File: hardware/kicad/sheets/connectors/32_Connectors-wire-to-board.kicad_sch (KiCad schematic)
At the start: 46 parts

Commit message: reorganized
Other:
- title: Connectors-wire-to-board -> Board IO Connectors

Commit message: before final cleanup
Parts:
- renumbered -12V+_6 to -12V+_5, -12V+_5 to -12V+_6, C301 to C107, C302 to C108, C105 to C109, C106 to C110, C107 to C111, C108 to C112, C308 to C113, C307 to C114, C309 to C115, C109 to C116, C110 to C117, C310 to C118, C160 to C119, C311 to C120, C306 to C121, C305 to C122, C304 to C123, C303 to C124, D85 to D30, D13 to D31, D14 to D32, D15 to D33, D84 to D34, D86 to D35, R555 to R159, R553 to R160, R552 to R161, R540 to R162, R541 to R163, R547 to R164, R542 to R165, R543 to R166, R550 to R167, R551 to R168, R554 to R169, R546 to R170, R544 to R171, R545 to R172, R549 to R173, R548 to R174, R556 to R175

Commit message: imrpved footprints
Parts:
- -12V+_4, -12V+_5, -12V+_6: footprint 5v rail sm-easyedapro:CONN-TH_2P-P3.96_VH3.96-2AW -> Connector_JST:JST_VH_B2P-VH_1x02_P3.96mm_Vertical
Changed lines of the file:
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@@
 			)
 		)
-		(property "Footprint" "5v rail sm-easyedapro:CONN-TH_2P-P3.96_VH3.96-2AW"
+		(property "Footprint" "Connector_JST:JST_VH_B2P-VH_1x02_P3.96mm_Vertical"
 			(at 363.22 149.86 0)
 			(effects
@@
 			)
 		)
-		(property "Footprint" "5v rail sm-easyedapro:CONN-TH_2P-P3.96_VH3.96-2AW"
+		(property "Footprint" "Connector_JST:JST_VH_B2P-VH_1x02_P3.96mm_Vertical"
 			(at 22.86 165.1 0)
 			(effects
@@
 			)
 		)
-		(property "Footprint" "5v rail sm-easyedapro:CONN-TH_2P-P3.96_VH3.96-2AW"
+		(property "Footprint" "Connector_JST:JST_VH_B2P-VH_1x02_P3.96mm_Vertical"
 			(at 284.48 106.68 0)
 			(effects

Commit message: added better footprints and steps
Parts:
- removed -12V+_4, -12V+_5, -12V+_6: VH3.96-2P WZ, Connector_JST:JST_VH_B2P-VH_1x02_P3.96mm_Vertical, symbol 5v rail sm-easyedapro:VH3.96-2P WZ
- removed C107, C114, C122, C124: 10uF, Capacitor_SMD:C_0805_2012Metric, symbol 5v rail sm-easyedapro:GRM21BR61H106KE43L
- removed C108, C113, C121, C123: 100nF, Capacitor_SMD:C_0603_1608Metric, symbol 5v rail sm-easyedapro:CC0603KRX7R9BB104
- removed C115, C118, C120: 10nF, Capacitor_SMD:C_0201_0603Metric, symbol 5v rail sm-easyedapro:TCC0201X7R103K500ZT
- removed CUR_4: INA3221AIRGVR, Package_DFN_QFN:QFN-16-1EP_4x4mm_P0.65mm_EP2.2x2.2mm, symbol 5v rail sm-easyedapro:INA3221AIRGVR
- removed D30, D34, D35: SMF13A, Diode_SMD:SOD-123FL, symbol 5v rail sm-easyedapro:SMF13A_C353315
- removed R159, R169, R175: 16mΩ, Resistor_SMD:R_2512_6332Metric, symbol 5v rail sm-easyedapro:LR123WF160MT4E
- removed R160, R161, R167, R168, R173, R174: 0Ω, Resistor_SMD:R_0201_0603Metric, symbol 5v rail sm-easyedapro:RC0201FR-070RL
- removed R162, R163, R165, R166, R171, R172: 10Ω, Resistor_SMD:R_0402_1005Metric, symbol 5v rail sm-easyedapro:RC0402FR-0710RL
- removed R164, R170: 10kΩ, Resistor_SMD:R_0402_1005Metric, symbol 5v rail sm-easyedapro:0402WGF1002TCE
- removed ___-3V3+_______-5V0+_______-12V+_______-VCC+___1: DB142R-5.08-8P-GN, 5v rail sm-easyedapro:CONN-TH_8P-P5.08_DIBO_DB142R-5.08-8P, symbol 5v rail sm-easyedapro:DB142R-5.08-8P
- added CN12: DB142R-5_08-8P, JLCImport:DB142R-5_08-8P, symbol JLCImport:DB142R-5_08-8P
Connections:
- net +12V: now also CN12.3
- net +3V3: now also CN12.7
- net +5V: now also CN12.5
- net GND: now also CN12.2, CN12.4, CN12.6, CN12.8
- net VCC: now also CN12.1
- no-connect marks 1 -> 0
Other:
- note removed: "0x40"

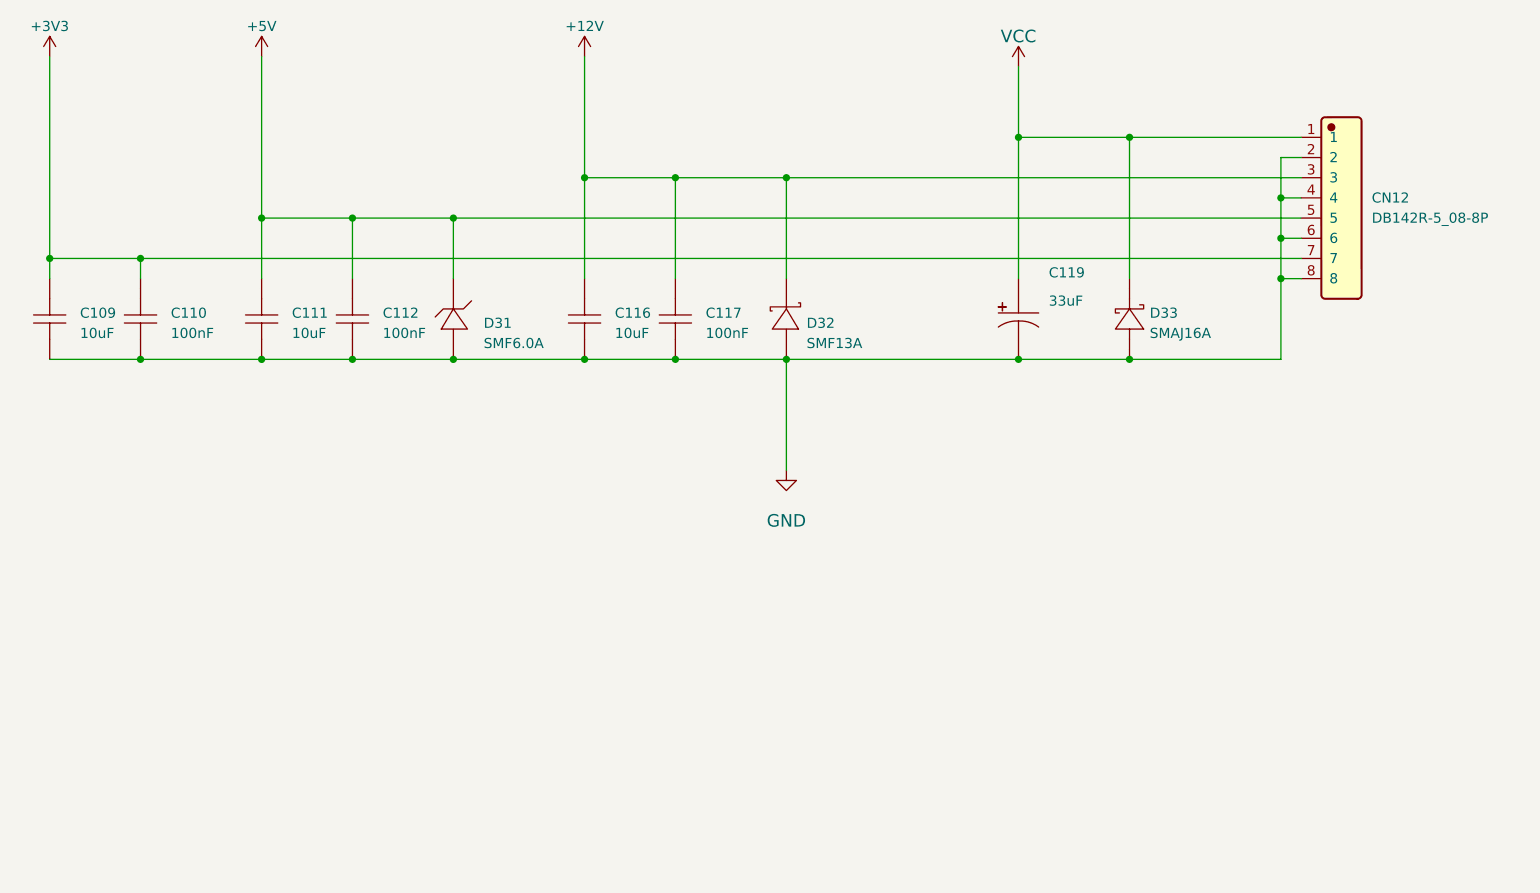
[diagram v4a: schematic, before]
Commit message: better sheet nesting for power rails
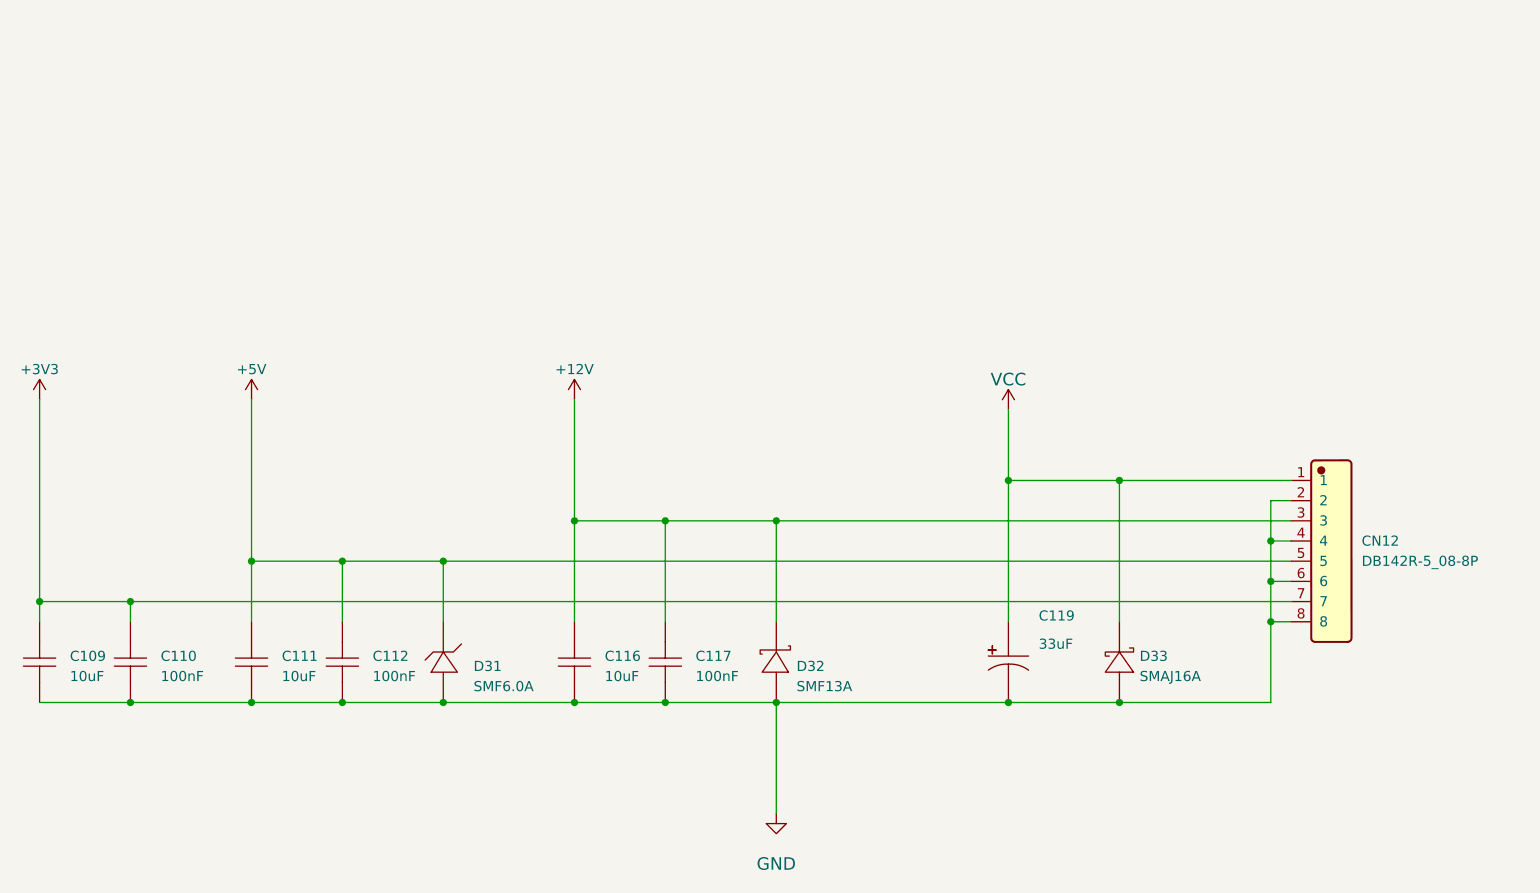
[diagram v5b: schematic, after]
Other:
- moved on the sheet: C109, C110, C111, C112, C116, C117, C119, CN12, D31, D32, D33

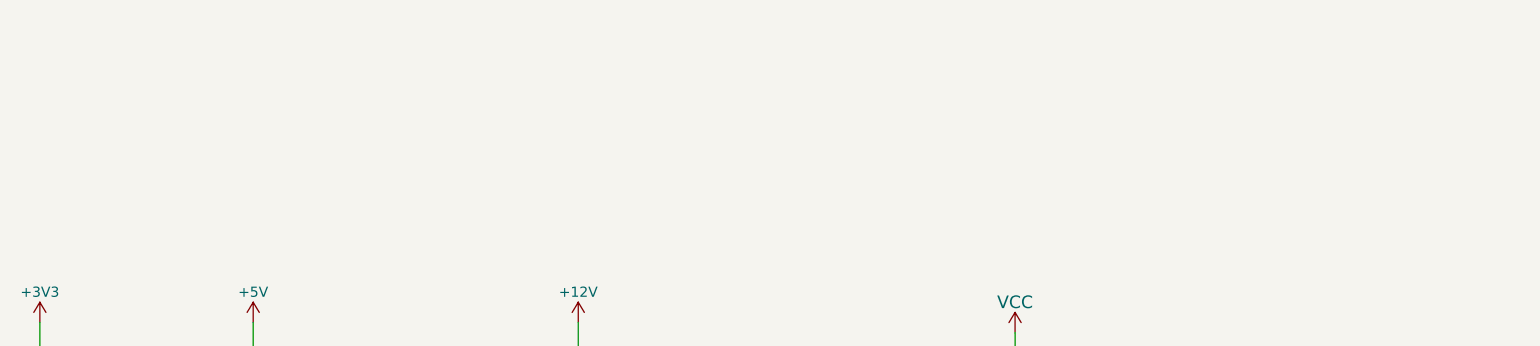
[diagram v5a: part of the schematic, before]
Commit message: clearer power path with sheets
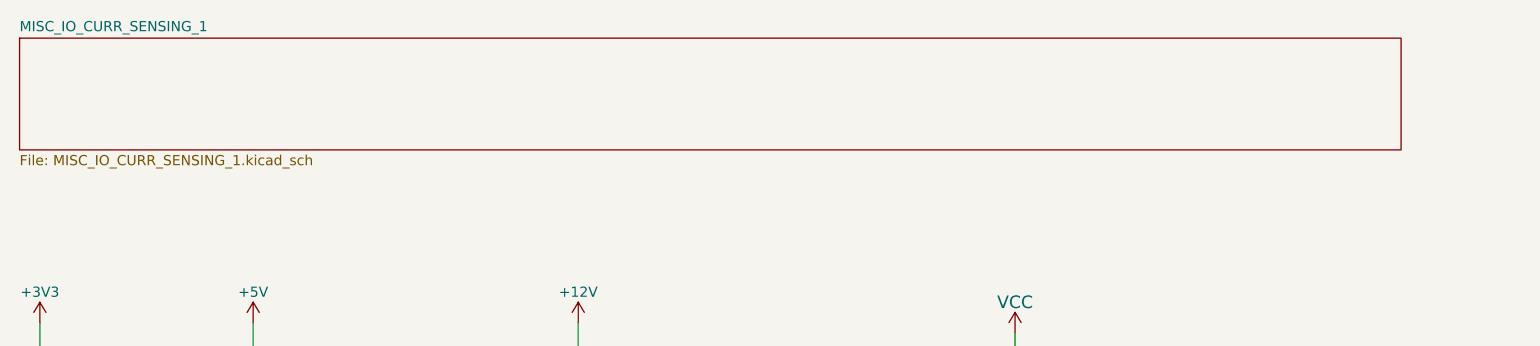
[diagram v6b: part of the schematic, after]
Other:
- added sheet MISC_IO_CURR_SENSING_1 (MISC_IO_CURR_SENSING_1.kicad_sch)
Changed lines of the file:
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@@
+		)
+	)
+	(sheet
+		(at 95.25 31.75)
+		(size 172.72 13.97)
+		(exclude_from_sim no)
+		(in_bom yes)
+		(on_board yes)
+		(dnp no)
+		(fields_autoplaced yes)
+		(stroke
+			(width 0.1524)
+			(type solid)
+		)
+		(fill
+			(color 0 0 0 0.0000)
+		)
+		(property "Sheetname" "MISC_IO_CURR_SENSING_1"
+			(at 95.25 31.0384 0)
+			(effects
+				(font
+					(size 1.27 1.27)
+				)
+				(justify left bottom)
+			)
+		)
+		(property "Sheetfile" "MISC_IO_CURR_SENSING_1.kicad_sch"
+			(at 95.25 46.3046 0)
+			(effects
+				(font
+					(size 1.27 1.27)
+				)
+				(justify left top)
+			)
+		)
+		(instances
+			(project "svea_powerboard_rev3"
+				(path "/3f85abf4-0b95-4c4a-b7e9-06f59ca1ea3d/5c2e021f-c2d4-49e2-8c36-9a64f1f12005/8d05c3b8-20a4-4a7f-9b20-01f8d5d5be51/d2f9c6a1-10e3-4d4e-9da8-c4d6204f6532"
+					(page "32")
+				)
+			)
 		)
 	)

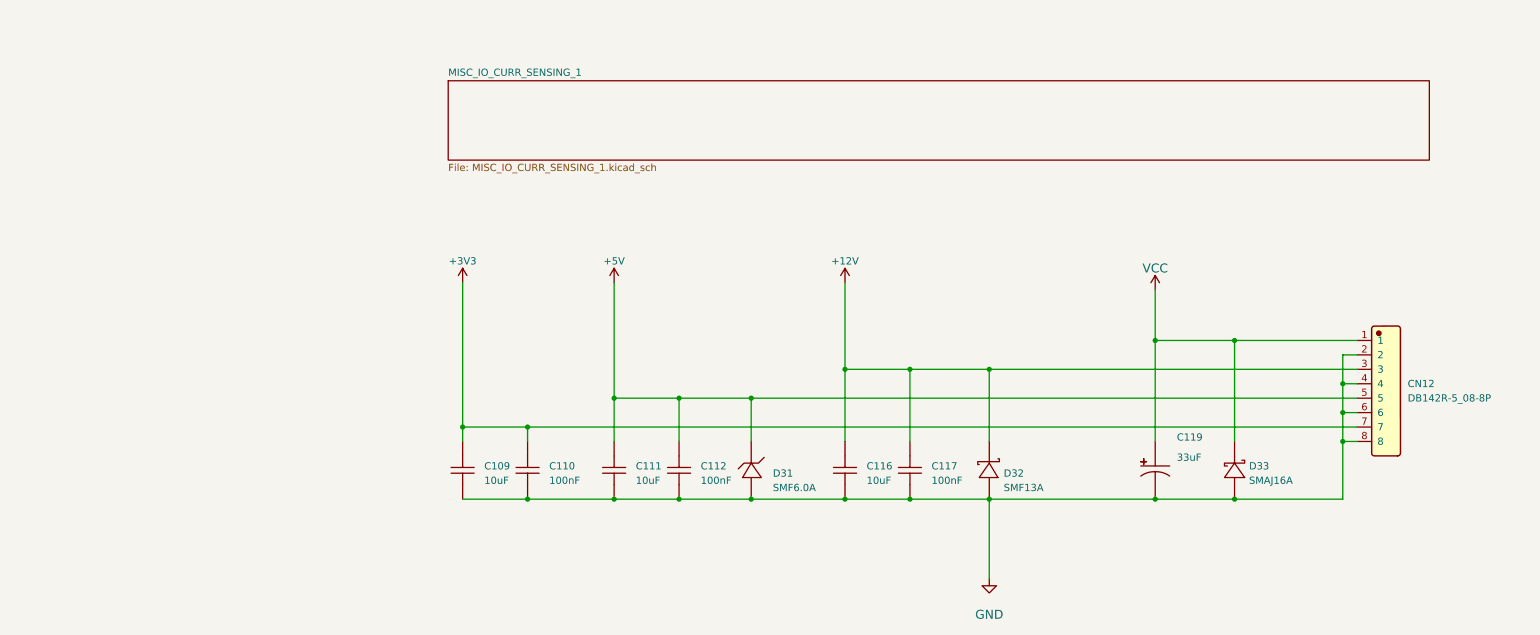
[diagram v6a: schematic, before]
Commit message: sheet optimized ports and current sensor
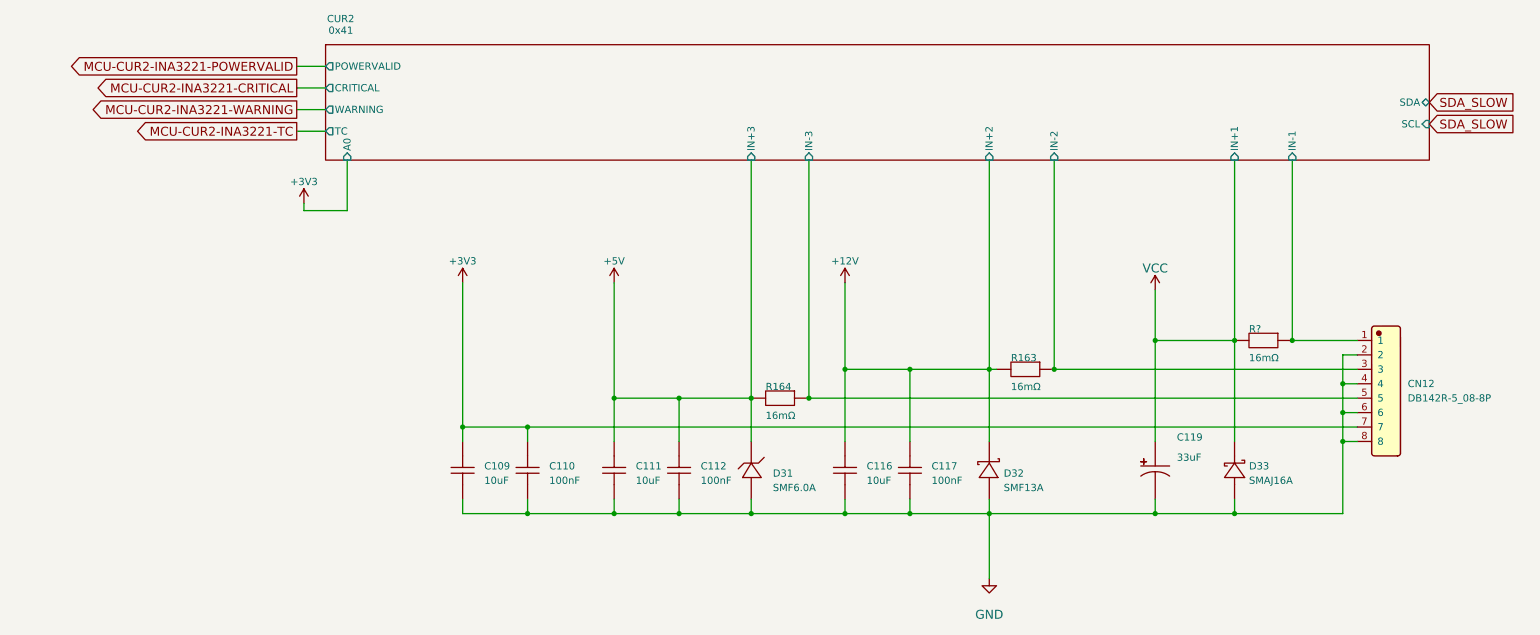
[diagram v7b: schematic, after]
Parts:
- added R163, R164, R?: 16mΩ, Resistor_SMD:R_2512_6332Metric, symbol 5v rail sm-easyedapro:LR123WF160MT4E
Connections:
- net +12V: now also R163.2; no longer CN12.3
- net +5V: now also R164.2; no longer CN12.5
- net VCC: now also D33.1, R?.2; no longer CN12.1
- new net CUR2/IN-1: CN12.1, R?.1
- new net CUR2/IN-2: CN12.3, R163.1
- new net CUR2/IN-3: CN12.5, R164.1
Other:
- sheet MISC_IO_CURR_SENSING_1 renamed CUR2
- sheet CUR2 ports: added A0, CRITICAL, IN+1, IN+2, IN+3, IN-1, IN-2, IN-3, POWERVALID, SCL, SDA, TC, WARNING; removed none
- note added: "0x41"
